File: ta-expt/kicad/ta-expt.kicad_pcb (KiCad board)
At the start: 4 copper layers, 45 x 45 mm, 34 parts, among them IC1 STM32L496RGT3, IC2 IS25LP128F-JBLA3, J1 Conn_01x16, J2 Conn_01x16, J3 Conn_01x04, J4 Conn_02x06_Odd_Even, J5 Conn_01x04, Q1 FDY300NZ, Q2 FDY300NZ, Y1 ABM8AIG-16.000MHZ-12-2Z-T, Y2 ABS07AIG-32.768kHz-T

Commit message: Updates Tartan Artibeus experiment board silkscreen labels
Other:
- board text added: "3V3"
- board text added: "LP.CTS"
- board text added: "LP.RTS"
- board text added: "LP.RX"
- board text added: "LP.TX"
- board text added: "SWCLK"
- board text added: "SWDIO"

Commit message: Tartan Artibeus experiment board v0.1.0
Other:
- board text added: "TA EXPT v0.1.0"

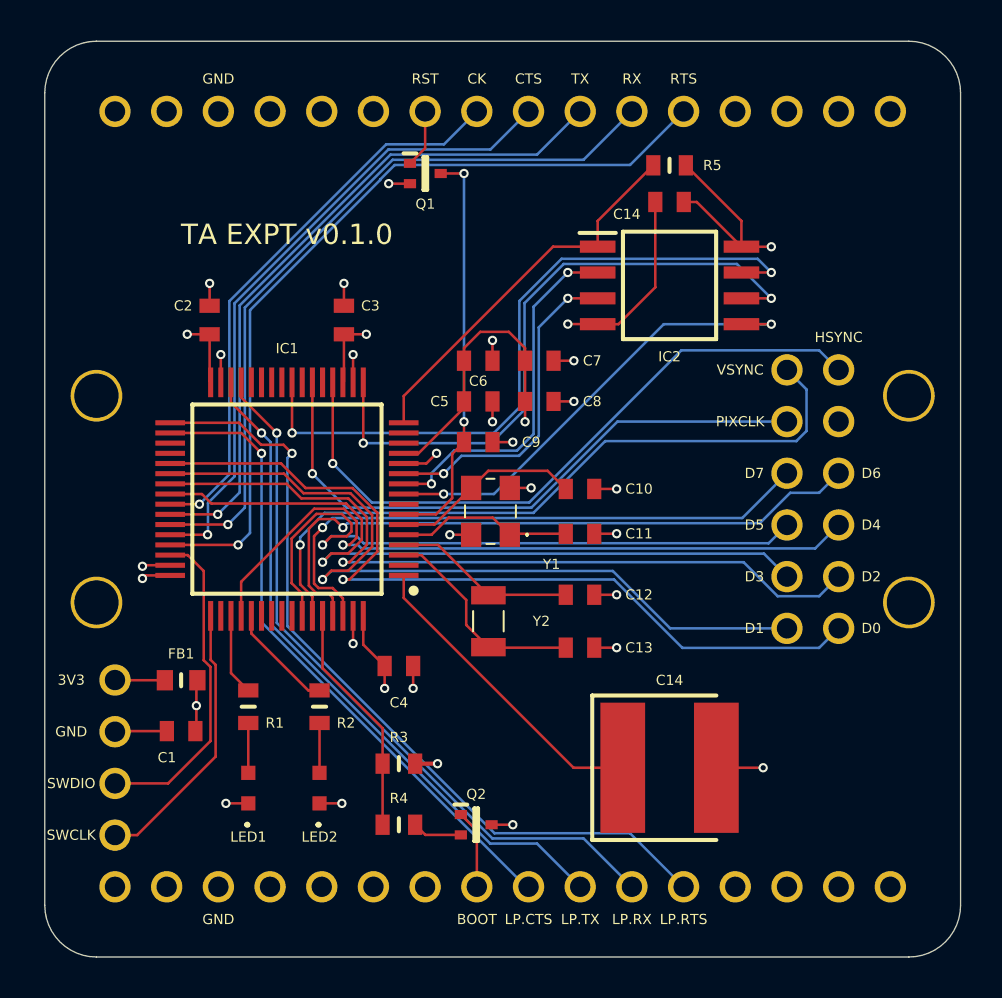
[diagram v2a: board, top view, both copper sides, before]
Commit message: Tartan Artibeus experiment board v1.0.0
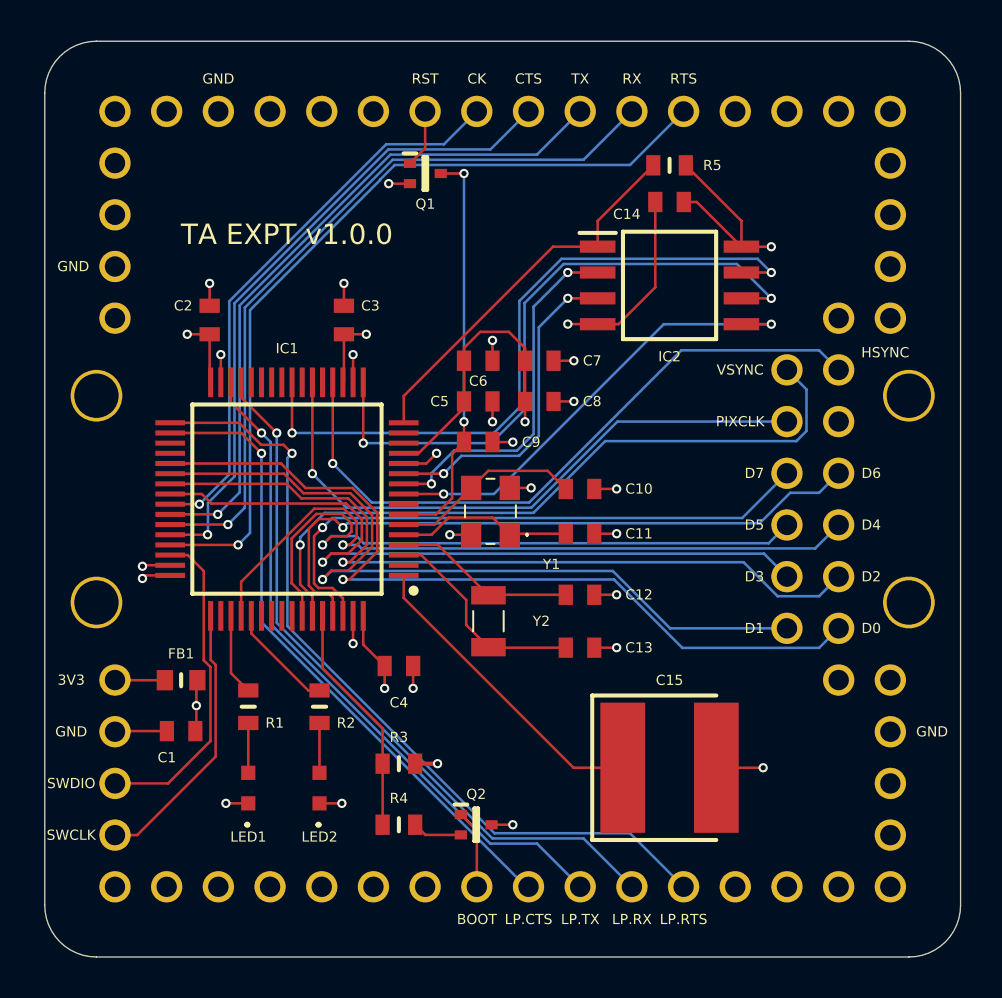
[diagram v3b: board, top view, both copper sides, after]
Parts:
- added J3: Conn_01x04, ta-expt:PinSocket_4x1_TartanArtibeus, F.Cu at (135.9, 95.3)
- added J5: Conn_01x05, ta-expt:PinSocket_1x5_TartanArtibeus, F.Cu at (174.1, 95.3)
- added J6: Conn_01x05, ta-expt:PinSocket_1x5_TartanArtibeus, B.Cu at (174.1, 120.7)
- renumbered J3 to J4, J5 to J7, J4 to J8
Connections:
- J2 pad 3: GND -> Net-(J2-Pad3)
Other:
- board text added: "C15"
- board text added: "TA EXPT v1.0.0"
- board text removed: "TA EXPT v0.1.0"

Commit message: Tartan Artibeus experiment board v1.0.1
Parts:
- removed Q1, Q2: FDY300NZ, ta-expt:SOTFL50P160X78-3N
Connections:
- J1 pad 7: /RST -> /NRST
- R4 pad 1: Net-(Q2-Pad2) -> /BOOT0
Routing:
- net /RST: track 2.86 -> 0.00 mm
- net /NRST: track 20.0 -> 22.7 mm
- net Net-(Q2-Pad2): track 2.45 -> 0.00 mm
- net GND: track 40.5 -> 39.5 mm, vias 25 -> 24
- net /VDD_FILT: track 40.4 -> 39.4 mm, vias 8 -> 7
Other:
- board text added: "NRST"
- board text added: "TA EXPT v1.0.1"
- board text removed: "Q1"
- board text removed: "Q2"
- board text removed: "RST"
- board text removed: "TA EXPT v1.0.0"
